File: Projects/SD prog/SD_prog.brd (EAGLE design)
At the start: 11 x 24.6 mm, 2 parts

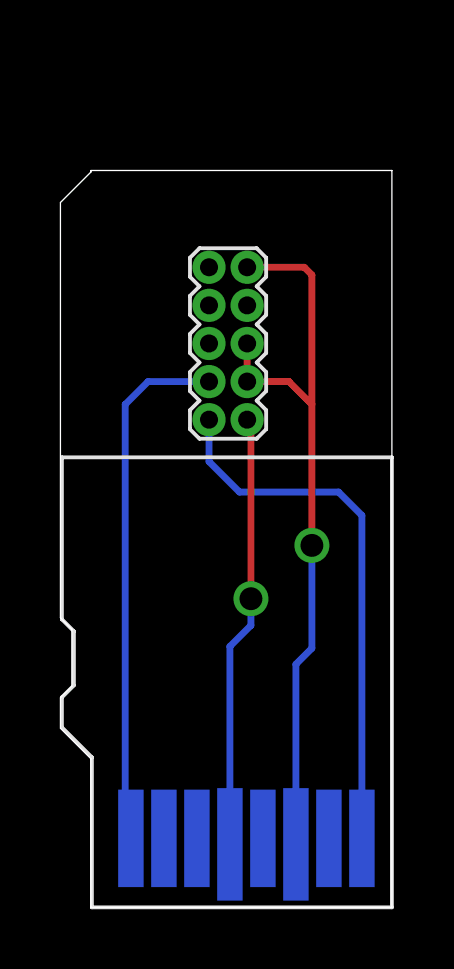
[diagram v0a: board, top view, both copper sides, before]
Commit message: Added buttons on ZLL Added pads on nRF51 key SD prog finished N5 lib updated
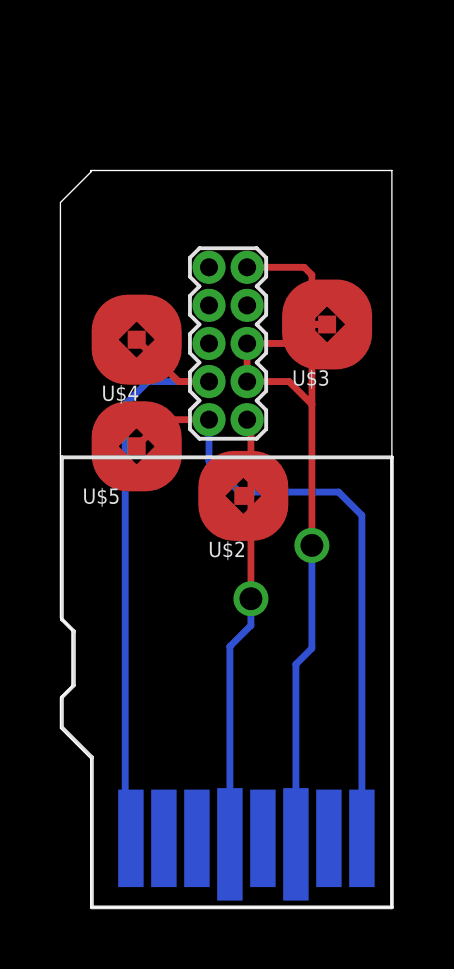
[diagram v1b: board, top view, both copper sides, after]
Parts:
- added U$2, U$3, U$4, U$5: TESTPOINT_33, test_points:TESTPOINT_33
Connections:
- net GND: now also U$3.P$1
- net SWDCLK/TCK: now also U$4.P$1
- net SWDIO/TMS: now also U$5.P$1
- net VCC: now also U$2.P$1
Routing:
- net SWDCLK/TCK: track 17.7 -> 20.6 mm
- net GND: track 25.2 -> 28.1 mm
- net SWDIO/TMS: track 18.0 -> 20.8 mm
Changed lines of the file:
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@@
 </element>
 <element name="U$1" library="con-cortex" package="2X5_0.05&quot;_TH_NS" value="2X5_0.05&quot;_CORTEX_DEBUGTH_NOKEY_UNSHROUDED" x="4.572" y="18.796" smashed="yes" rot="R90"/>
+<element name="U$2" library="test_points" package="TESTPOINT_33" value="TESTPOINT_33" x="5.08" y="13.716" smashed="yes">
+<attribute name="NAME" x="3.91" y="11.676" size="0.508" layer="21"/>
+</element>
+<element name="U$3" library="test_points" package="TESTPOINT_33" value="TESTPOINT_33" x="7.874" y="19.431" smashed="yes">
+<attribute name="NAME" x="6.704" y="17.391" size="0.508" layer="21"/>
+</element>
+<element name="U$4" library="test_points" package="TESTPOINT_33" value="TESTPOINT_33" x="1.524" y="18.923" smashed="yes">
+<attribute name="NAME" x="0.354" y="16.883" size="0.508" layer="21"/>
+</element>
+<element name="U$5" library="test_points" package="TESTPOINT_33" value="TESTPOINT_33" x="1.524" y="15.367" smashed="yes">
+<attribute name="NAME" x="-0.281" y="13.454" size="0.508" layer="21"/>
+</element>
 </elements>
 <signals>
@@
 <wire x1="5.334" y1="9.398" x2="5.334" y2="10.287" width="0.2286" layer="16"/>
 <via x="5.334" y="10.287" extent="1-16" drill="0.762"/>
-<wire x1="5.334" y1="10.287" x2="5.334" y2="16.129" width="0.2286" layer="1"/>
-<wire x1="5.334" y1="16.129" x2="5.207" y2="16.256" width="0.2286" layer="1"/>
+<contactref element="U$2" pad="P$1"/>
+<wire x1="5.207" y1="16.256" x2="5.334" y2="16.129" width="0.2286" layer="1"/>
+<wire x1="5.334" y1="16.129" x2="5.334" y2="10.287" width="0.2286" layer="1"/>
+<wire x1="5.207" y1="16.256" x2="5.08" y2="13.716" width="0" layer="19" extent="1-1"/>
 </signal>
 <signal name="SWDIO/TMS">
@@
 <wire x1="9.033" y1="13.065" x2="8.255" y2="13.843" width="0.2286" layer="16"/>
 <wire x1="3.937" y1="14.859" x2="3.937" y2="16.256" width="0.2286" layer="16"/>
+<contactref element="U$5" pad="P$1"/>
+<wire x1="3.937" y1="16.256" x2="2.413" y2="16.256" width="0.2286" layer="1"/>
+<wire x1="2.413" y1="16.256" x2="1.524" y2="15.367" width="0.2286" layer="1"/>
 </signal>
 <signal name="SWDCLK/TCK">
@@
 <wire x1="1.143" y1="16.764" x2="1.143" y2="2.49" width="0.2286" layer="16"/>
 <wire x1="1.143" y1="2.49" x2="1.333" y2="2.3" width="0.2286" layer="16"/>
+<contactref element="U$4" pad="P$1"/>
+<wire x1="3.937" y1="17.526" x2="2.921" y2="17.526" width="0.2286" layer="1"/>
+<wire x1="2.921" y1="17.526" x2="1.524" y2="18.923" width="0.2286" layer="1"/>
 </signal>
 <signal name="GND">
@@
 <wire x1="7.112" y1="21.336" x2="7.366" y2="21.082" width="0.2286" layer="1"/>
 <wire x1="7.366" y1="21.082" x2="7.366" y2="16.764" width="0.2286" layer="1"/>
+<contactref element="U$3" pad="P$1"/>
+<wire x1="5.207" y1="18.796" x2="6.604" y2="18.796" width="0.2286" layer="1"/>
+<wire x1="7.239" y1="19.431" x2="7.874" y2="19.431" width="0.2286" layer="1"/>
+<wire x1="6.604" y1="18.796" x2="7.239" y2="19.431" width="0.2286" layer="1"/>
 </signal>
 </signals>

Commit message: Order @ Boktech
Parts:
- added U$6, U$7, U$8, U$9: TESTPOINT_22, test_points:TESTPOINT_22
- moved U$4 3.68 mm to (1.52, 22.6)
- moved U$2 3.68 mm to (5.08, 17.4)
- moved U$1 3.68 mm to (4.57, 22.5)
- moved U$3 3.68 mm to (7.87, 23.1)
- moved U$5 3.68 mm to (1.52, 19.1)
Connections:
- new net N$1: B1.CD/DAT3, U$6.P$1
- new net N$2: B1.CMD, U$7.P$1
- new net N$3: B1.CLK, U$8.P$1
- new net N$4: B1.DAT0, U$9.P$1
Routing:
- net N$3: track 0.00 -> 11.8 mm, vias 0 -> 1
- net N$1: track 0.00 -> 11.7 mm, vias 0 -> 1
- net N$2: track 0.00 -> 8.59 mm, vias 0 -> 1
- net N$4: track 0.00 -> 7.89 mm, vias 0 -> 1
- net VCC: track 14.5 -> 19.2 mm
- net SWDCLK/TCK: track 20.6 -> 24.3 mm
- net SWDIO/TMS: track 20.8 -> 24.5 mm
- net GND: track 28.1 -> 31.8 mm
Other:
- board size 11 x 24.6 mm -> 11 x 28.2 mm
